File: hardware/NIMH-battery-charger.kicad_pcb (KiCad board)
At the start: 2 copper layers, 7 parts, among them J1 USB_A

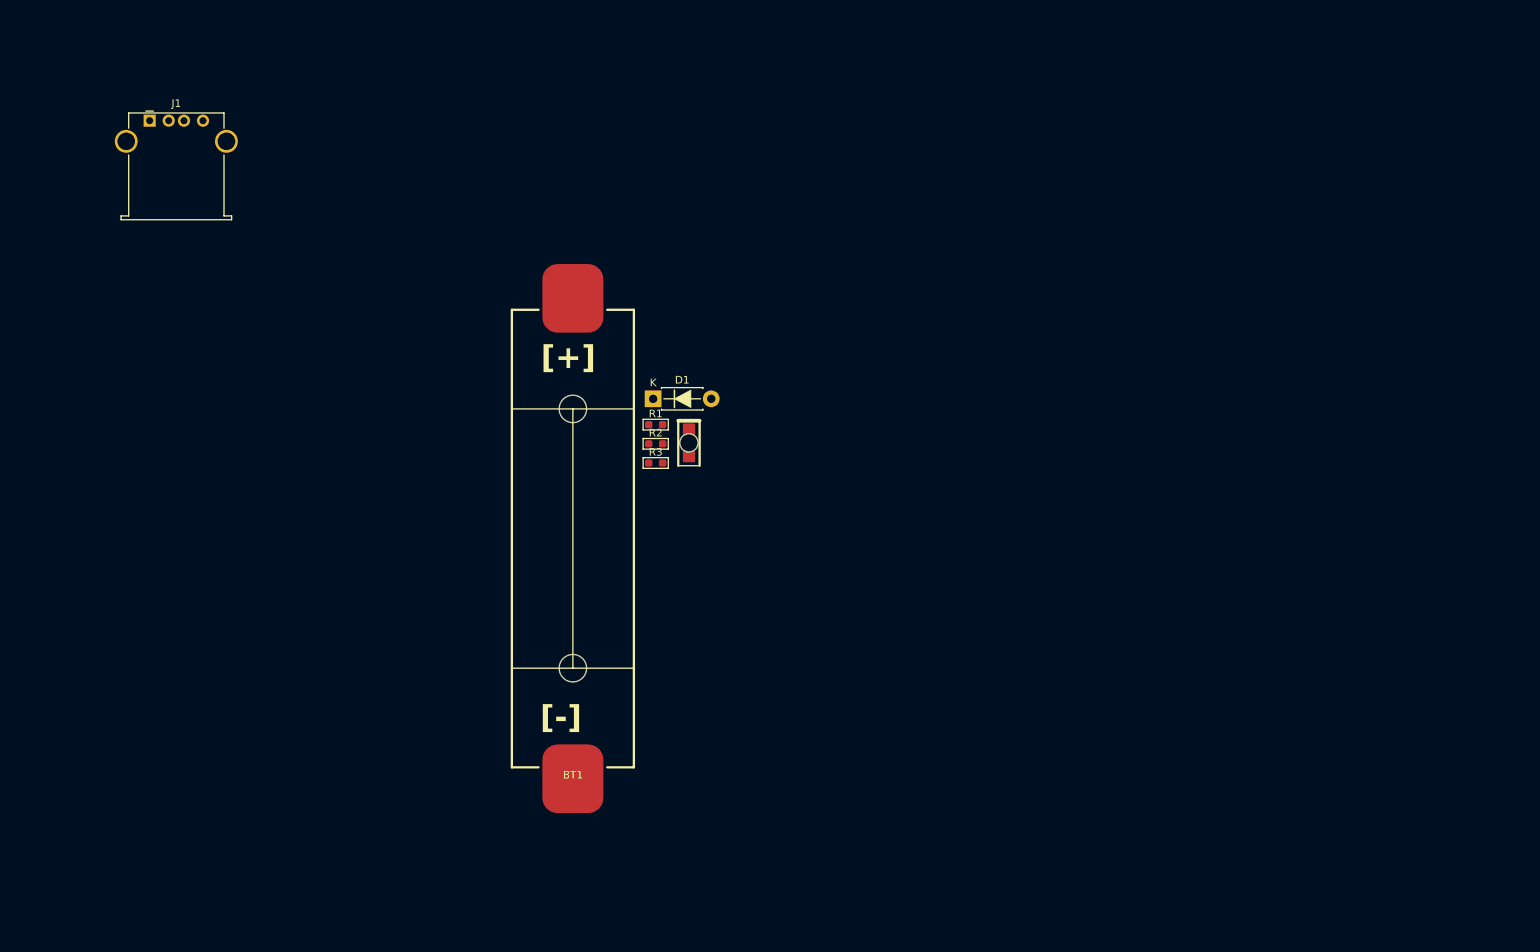
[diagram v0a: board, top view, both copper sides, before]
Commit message: Add comments for development board
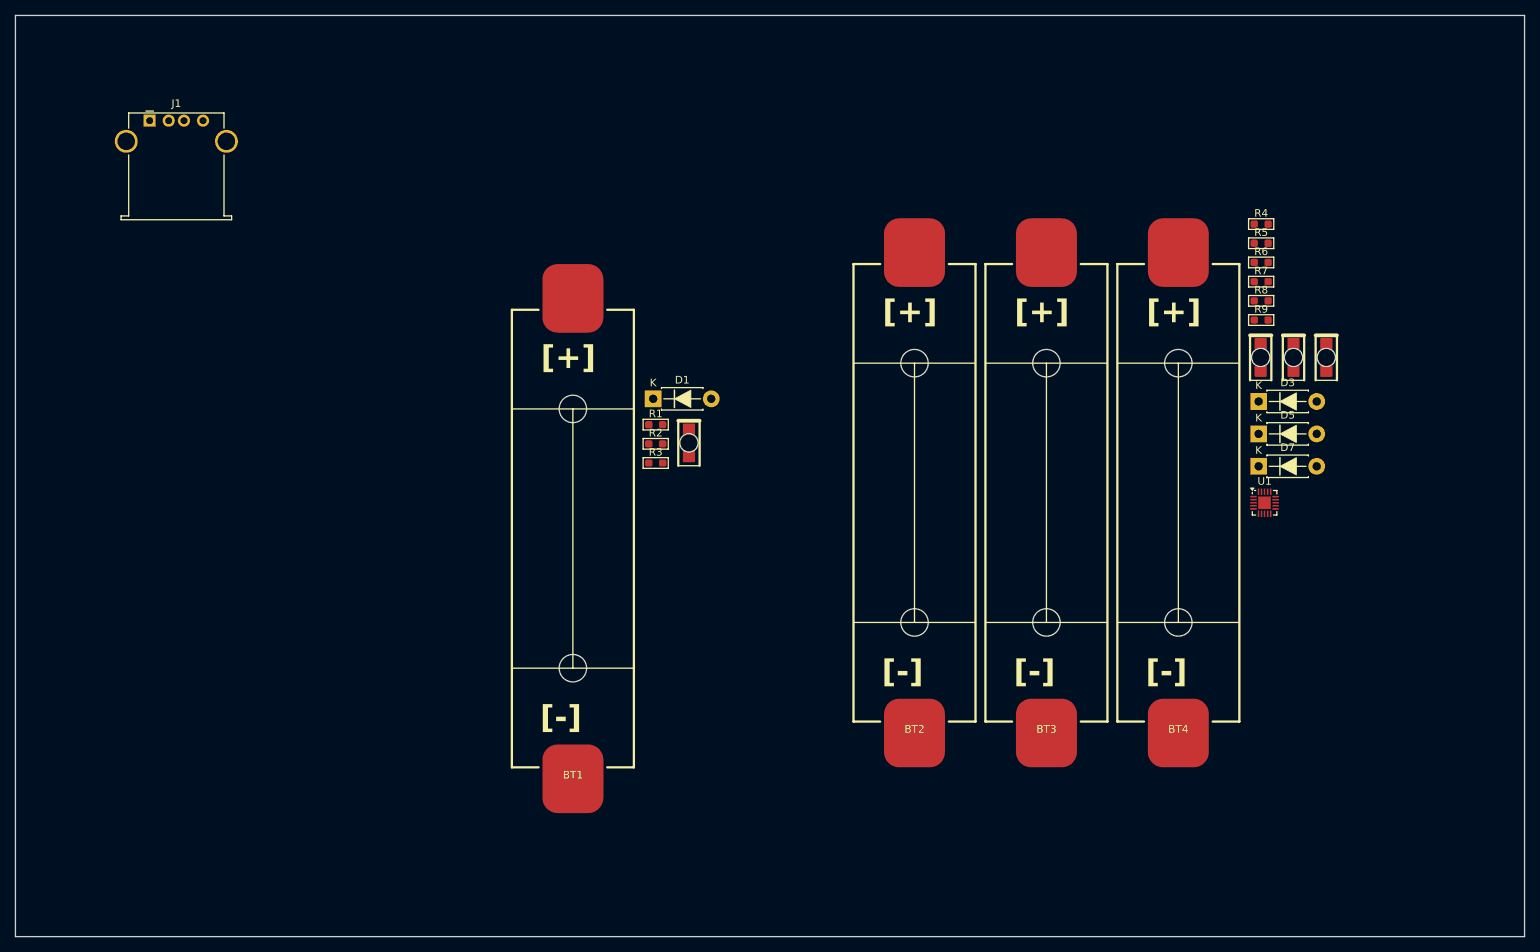
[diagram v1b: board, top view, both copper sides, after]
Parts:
- added BT2: Battery_Cell, Special_Local:UM-3X1-AA, F.Cu at (179.4, 120.2)
- added BT3: Battery_Cell, Special_Local:UM-3X1-AA, F.Cu at (196.7, 120.2)
- added BT4: Battery_Cell, Special_Local:UM-3X1-AA, F.Cu at (214.0, 120.2)
- added D3: 1N4001, PCM_Diode_THT_AKL:D_DO-41_SOD81_P7.62mm_Horizontal, F.Cu at (224.5, 76.7)
- added D4: LED, Special_Local:KPTR-3216SGC, F.Cu at (224.8, 72.8)
- added D5: 1N4001, PCM_Diode_THT_AKL:D_DO-41_SOD81_P7.62mm_Horizontal, F.Cu at (224.5, 81.0)
- added D6: LED, Special_Local:KPTR-3216SGC, F.Cu at (229.1, 72.8)
- added D7: 1N4001, PCM_Diode_THT_AKL:D_DO-41_SOD81_P7.62mm_Horizontal, F.Cu at (224.5, 85.2)
- added D8: LED, Special_Local:KPTR-3216SGC, F.Cu at (233.4, 72.8)
- added R4: 120R, PCM_Resistor_SMD_AKL:R_0603_1608Metric_Pad0.98x0.95mm_HandSolder, F.Cu at (224.9, 53.5)
- added R5: 120R, PCM_Resistor_SMD_AKL:R_0603_1608Metric_Pad0.98x0.95mm_HandSolder, F.Cu at (224.9, 56.0)
- added R6: 120R, PCM_Resistor_SMD_AKL:R_0603_1608Metric_Pad0.98x0.95mm_HandSolder, F.Cu at (224.9, 58.5)
- added R7: 120R, PCM_Resistor_SMD_AKL:R_0603_1608Metric_Pad0.98x0.95mm_HandSolder, F.Cu at (224.9, 61.0)
- added R8: 120R, PCM_Resistor_SMD_AKL:R_0603_1608Metric_Pad0.98x0.95mm_HandSolder, F.Cu at (224.9, 63.5)
- added R9: 120R, PCM_Resistor_SMD_AKL:R_0603_1608Metric_Pad0.98x0.95mm_HandSolder, F.Cu at (224.9, 66.0)
- added U1: CH32V003f4u6, Package_DFN_QFN:QFN-20-1EP_3x3mm_P0.4mm_EP1.65x1.65mm, F.Cu at (225.3, 90.0)
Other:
- board outline added: 197.9 x 120.8 mm

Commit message: Completing schematic and adding comments and images
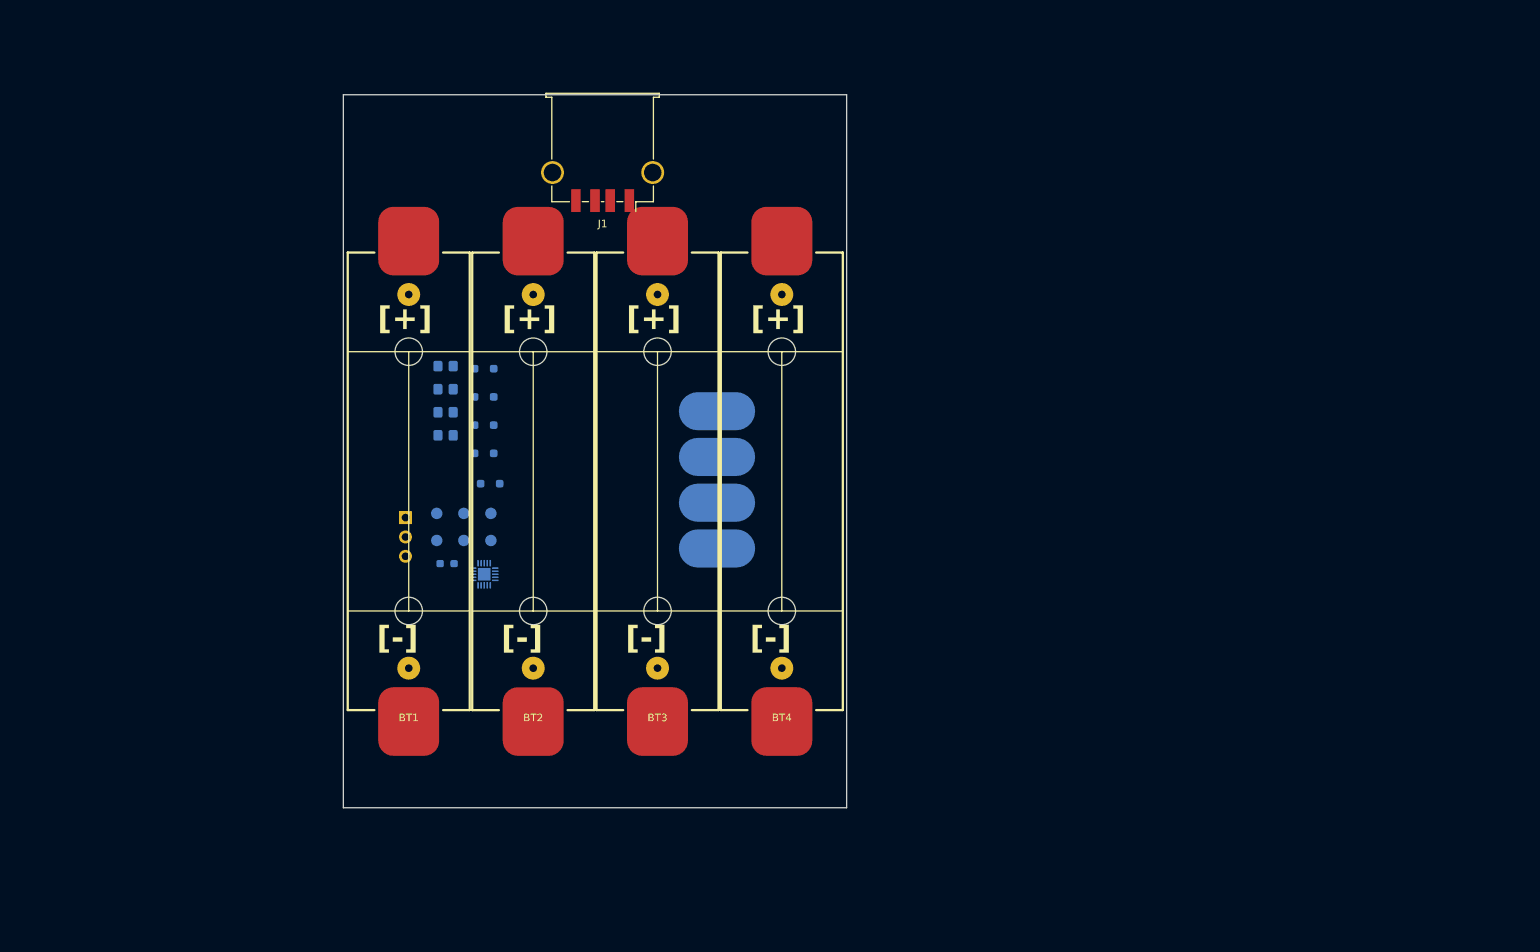
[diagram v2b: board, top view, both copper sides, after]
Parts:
- removed D5, D7: 1N4001, PCM_Diode_THT_AKL:D_DO-41_SOD81_P7.62mm_Horizontal
- removed D6, D8: LED, Special_Local:KPTR-3216SGC
- removed R6, R7, R8, R9: 120R, PCM_Resistor_SMD_AKL:R_0603_1608Metric_Pad0.98x0.95mm_HandSolder
- added D9: 1N4001, PCM_Diode_SMD_Handsoldering_AKL:D_SOD-323_BigPads, B.Cu at (123.8, 87.5)
- added J2: Conn_01x03_Pin, Connector_PinHeader_2.54mm:PinHeader_1x03_P2.54mm_Vertical, B.Cu at (112.7, 92.0)
- added J3: Conn_01x01_Pin, Special_Local:PAD, B.Cu at (153.5, 78.0)
- added J4: Conn_01x01_Pin, Special_Local:PAD, B.Cu at (153.5, 84.0)
- added J5: Conn_01x01_Pin, Special_Local:PAD, B.Cu at (153.5, 90.0)
- added J6: Conn_01x01_Pin, Special_Local:PAD, B.Cu at (153.5, 96.0)
- added TP1: TestPoint, TestPoint:TestPoint_Pad_D1.5mm, B.Cu at (123.8, 91.4)
- added TP2: TestPoint, TestPoint:TestPoint_Pad_D1.5mm, B.Cu at (123.8, 95.0)
- added TP3: TestPoint, TestPoint:TestPoint_Pad_D1.5mm, B.Cu at (120.3, 91.4)
- added TP4: TestPoint, TestPoint:TestPoint_Pad_D1.5mm, B.Cu at (120.3, 95.0)
- added TP5: TestPoint, TestPoint:TestPoint_Pad_D1.5mm, B.Cu at (116.8, 91.4)
- added TP6: TestPoint, TestPoint:TestPoint_Pad_D1.5mm, B.Cu at (116.8, 95.0)
- BT1, BT2, BT3, BT4: value Battery_Cell -> Battery
- D1, D3: footprint PCM_Diode_THT_AKL:D_DO-41_SOD81_P7.62mm_Horizontal -> PCM_Diode_SMD_Handsoldering_AKL:D_SOD-323_BigPads; moved to B.Cu
- D2, D4: value LED -> 1N4001; footprint Special_Local:KPTR-3216SGC -> PCM_Diode_SMD_Handsoldering_AKL:D_SOD-323_BigPads; moved to B.Cu
- J1: footprint Connector_USB:USB_A_Stewart_SS-52100-001_Horizontal -> Connector_USB:USB_A_TE_292303-7_Horizontal
- R1, R2, R4, R5: value 120R -> 100R; footprint PCM_Resistor_SMD_AKL:R_0603_1608Metric_Pad0.98x0.95mm_HandSolder -> PCM_Resistor_SMD_AKL:R_0805_2012Metric_Pad1.20x1.40mm_HandSolder; moved to B.Cu
- R3, U1: moved to B.Cu
- moved R5 109.9 mm to (117.9, 81.2), turned to 180 degrees
- moved R4 109.8 mm to (117.9, 78.1), turned to 180 degrees
- moved U1 102.8 mm to (123.0, 99.4), turned to 180 degrees
- moved D4 102.4 mm to (123.0, 83.5), turned to 180 degrees
- moved D3 101.6 mm to (123.0, 79.8), turned to 180 degrees
- moved J1 59.5 mm to (138.5, 44.0), turned to 180 degrees
- moved BT4 52.0 mm to (162.0, 118.7)
- moved BT3 51.0 mm to (145.7, 118.7)
- moved BT2 50.0 mm to (129.4, 118.7)
- moved R3 30.4 mm to (118.1, 98.0), turned to 180 degrees
- moved R1 28.6 mm to (117.9, 72.1), turned to 180 degrees
- moved R2 28.5 mm to (117.9, 75.1), turned to 180 degrees
- moved D2 28.0 mm to (123.0, 76.1), turned to 180 degrees
- moved BT1 22.8 mm to (113.1, 118.7)
- moved D1 22.5 mm to (123.0, 72.4), turned to 180 degrees
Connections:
- BT1 pad 1: Net-(BT1-+) -> /ADC1
- BT2 pad 1: Net-(BT2-+) -> /ADC2
- BT3 pad 1: Net-(BT3-+) -> /ADC3
- BT4 pad 1: Net-(BT4-+) -> /ADC4
- D2 pad 2: Net-(D1-K) -> +5V
- D4 pad 2: Net-(D3-K) -> +5V
- R1 pad 2: Net-(BT1-+) -> /ADC1
- R2 pad 2: Net-(BT1-+) -> /ADC2
- R4 pad 2: Net-(BT2-+) -> /ADC3
- R5 pad 2: Net-(BT2-+) -> /ADC4
- U1 pad 1: unconnected-(U1-PD7_NRST_T2CH4-Pad1) -> /LED1
- U1 pad 10: unconnected-(U1-PC3-Pad10) -> Net-(U1-PC3)
- U1 pad 11: unconnected-(U1-PC4_A2_T1CH4-Pad11) -> /ADC1
- U1 pad 12: unconnected-(U1-PC5_SCK-Pad12) -> Net-(U1-PC5_SCK)
- U1 pad 13: unconnected-(U1-PC6_MOSI-Pad13) -> Net-(U1-PC6_MOSI)
- U1 pad 14: unconnected-(U1-PC7_MISO-Pad14) -> Net-(U1-PC7_MISO)
- U1 pad 15: unconnected-(U1-SWIO&PD1_T1CH3N-Pad15) -> /SWIO
- U1 pad 16: unconnected-(U1-PD2_A3_T2CH1-Pad16) -> /ADC2
- U1 pad 17: unconnected-(U1-PD2_A4_T1CH2-Pad17) -> /ADC3
- U1 pad 18: unconnected-(U1-PD4_A7_T2AETR2-Pad18) -> /ADC4
- U1 pad 19: unconnected-(U1-PD5_A5_UART_TX-Pad19) -> /UART_TX
- U1 pad 2: unconnected-(U1-PA1_A1_T1CH2_OSCI-Pad2) -> /LED2
- U1 pad 20: unconnected-(U1-PD6_A6_UART_RX-Pad20) -> /UART_RX
- U1 pad 3: unconnected-(U1-PA2_A0_T1CH2N_OSCO-Pad3) -> /LED3
- U1 pad 4: unconnected-(U1-vss-Pad4) -> GND
- U1 pad 5: unconnected-(U1-PD0_T1CH1N-Pad5) -> /LED4
- U1 pad 6: unconnected-(U1-VDD-Pad6) -> VDD
- U1 pad 7: unconnected-(U1-PC0_T2CH3-Pad7) -> /LED0
- U1 pad 8: unconnected-(U1-PC1_SDA-Pad8) -> Net-(U1-PC1_SDA)
- U1 pad 9: unconnected-(U1-PC2_SCL-Pad9) -> Net-(U1-PC2_SCL)
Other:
- board size 197.9 x 120.8 mm -> 66 x 93.5 mm

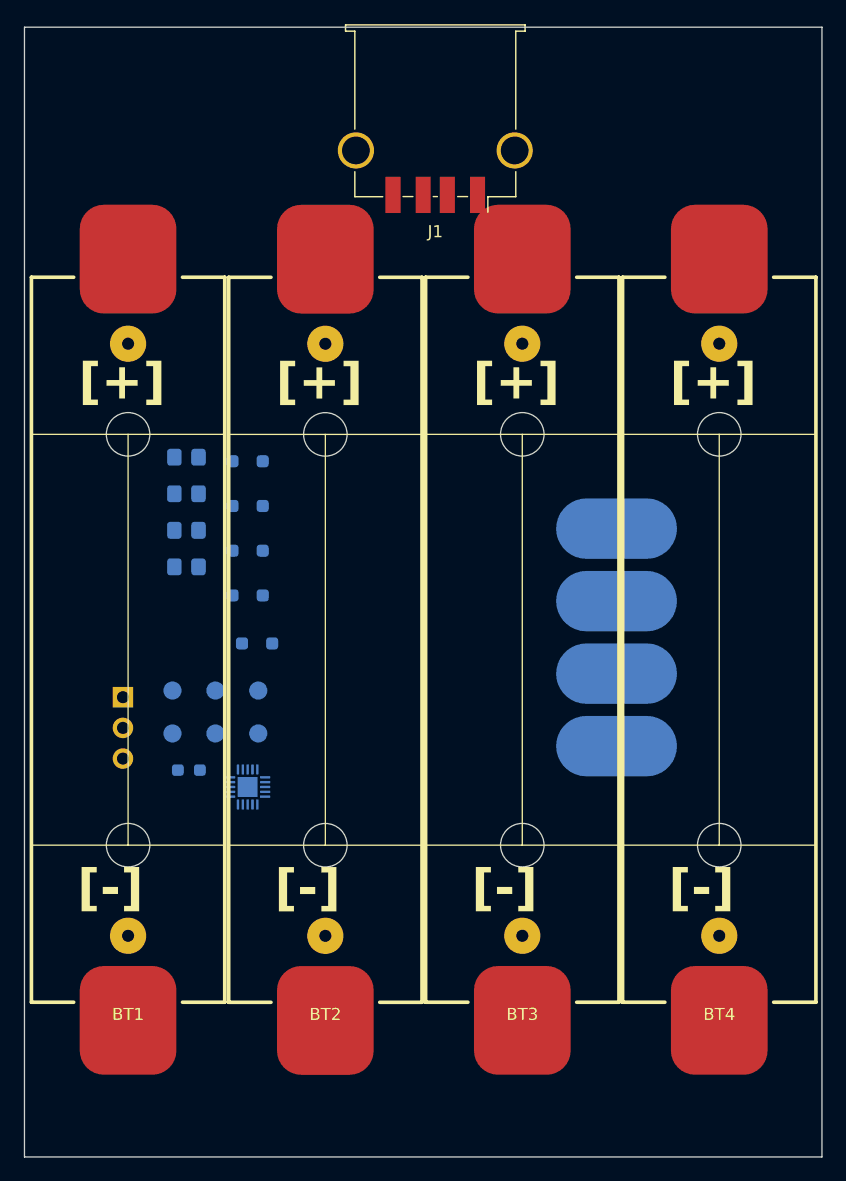
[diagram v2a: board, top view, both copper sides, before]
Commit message: Add USB_C receptacle
Add documents
Resizing the board
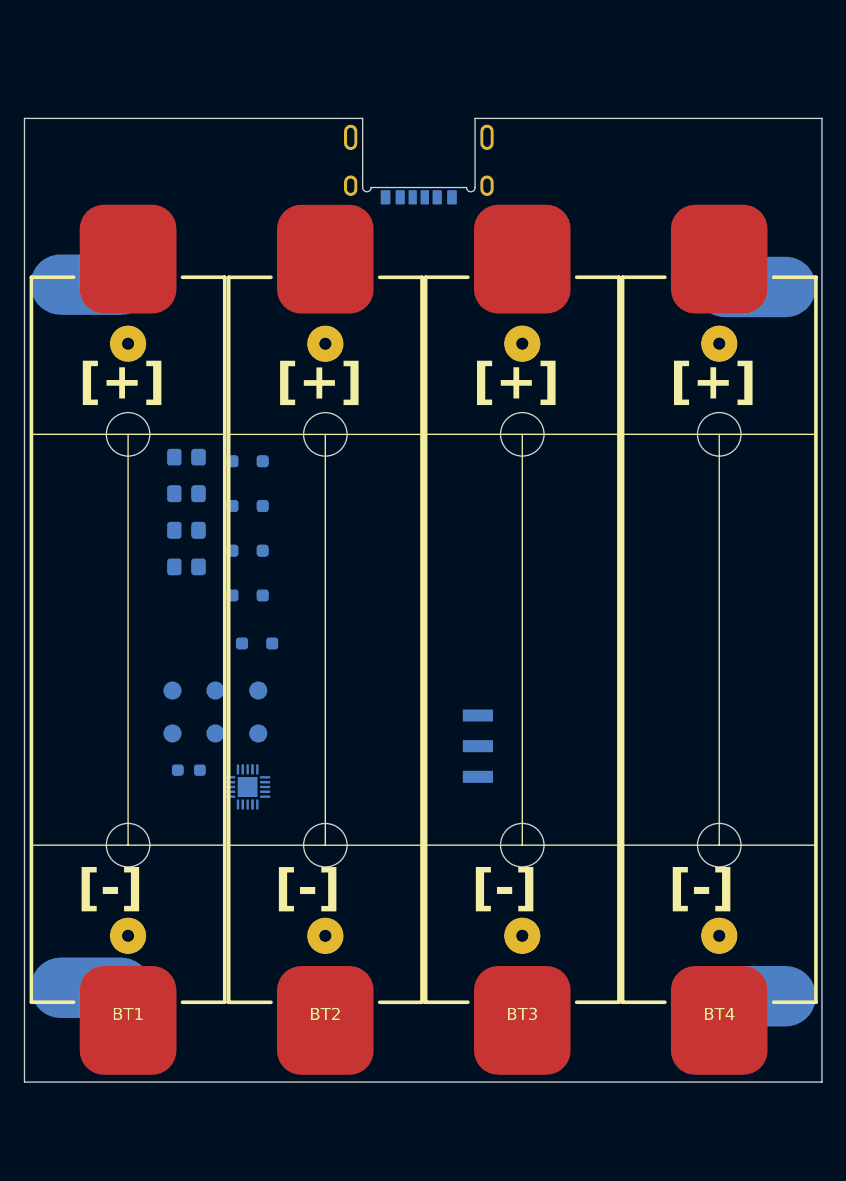
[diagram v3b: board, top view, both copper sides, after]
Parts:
- removed J2: Conn_01x03_Pin, Connector_PinHeader_2.54mm:PinHeader_1x03_P2.54mm_Vertical
- added J7: USB_C_Receptacle_PowerOnly_6P, Special_Local:USB4515-GF-A, B.Cu at (137.2, 47.4)
- J1: value USB_A -> Conn_01x03_Pin; footprint Connector_USB:USB_A_TE_292303-7_Horizontal -> Connector_Harwin:Harwin_M20-89003xx_1x03_P2.54mm_Horizontal; moved to B.Cu
- moved J5 54.1 mm to (110.0, 57.8)
- moved J1 52.0 mm to (136.5, 96.0)
- moved J6 47.9 mm to (110.0, 116.0)
- moved J4 34.7 mm to (165.0, 116.7)
- moved J3 23.1 mm to (165.0, 58.0)
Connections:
- J1 pad 1: +5V -> /SWIO
- J1 pad 2: unconnected-(J1-D--Pad2) -> VDD
- J1 pad 3: unconnected-(J1-D+-Pad3) -> GND
- R3 pad 1: Net-(J1-Shield) -> Net-(J7-SHIELD)
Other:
- board size 66 x 93.5 mm -> 66 x 79.8 mm
